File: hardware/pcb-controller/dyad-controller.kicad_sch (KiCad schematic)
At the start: 36 parts, among them J1 USB_C_Receptacle_USB2.0, J2 SWD, J3 Conn_01x11, J4 Conn_01x11, J5 Conn_01x11, SW1 SW_Push, U1 W25Q128JVS, U2 USBLC6-2SC6, U3 RP2040, U4 XC6206PxxxMR-Regulator_Linear, Y1 12MHz

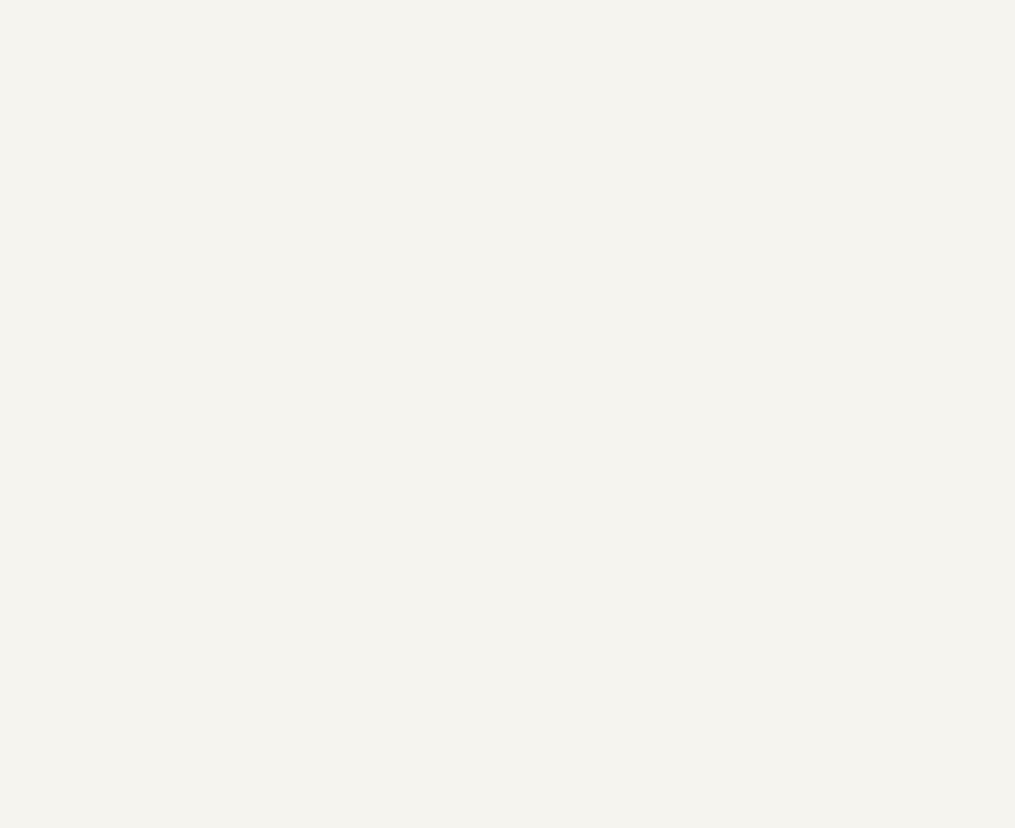
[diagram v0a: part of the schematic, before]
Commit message: Add both main FFC connectors to the controller schematic
J6 (left half) and J7 (right half), Connector_Generic:Conn_01x20 against the
C19273932 footprint, all 40 pins wired. The `dyad` library is registered in
the controller's fp-lib-table with the same relative URI the mains use.

Both carry the same net-to-pad assignment, derived pad by pad as
`pad m = main pin (21 - m)` rather than transcribed:

  1=HAND(GPIO12)  2=+3V3  3-10=COL7..COL0(GPIO26..19)
  11-15=ROW0..ROW4(GPIO14..18)  16,18=GND  17=LEDIN(GPIO13)  19,20=+5V

The 5 V pins land on **+5V, not VBUS**. VBUS -> F1 -> +5V, so +5V is the
fused rail, and §3 already notes the fuse is deliberately in the LED path --
which is the whole reason it needs upsizing if RGB is populated. Taking the
FFC's 5 V from VBUS would have put the LED current outside the fuse and
quietly defeated that. Verified by reading the net back: +5V now contains
F1 pin 2, the LDO input, the ESD part, the PWR_FLAG and both connectors.

The sheet moved A4 -> A3. Placed content already ran to x=282.6 on a 297 mm
frame, and two 20-pin connectors need 48 mm of pin span each, with the knob
FFC and second USB-C still to come.

This also corrects the pad table added in 4bcd259, which was garbled: it
repeated COL0-6 in both halves and omitted ROW3, ROW4, both GNDs, LEDIN and
both VCCs. It carried a "not verified" warning, which is the only reason it
did not reach copper. The corrected table gives the controller's own net
name per pad and carries a count check.

Numbers: ERC is byte-identical to baseline -- 192 violations, 0 errors, and
not one mentions J6 or J7. 40 pins added with no new findings. 0 shorts, 0
orphans. The 4 symbol overlaps are pre-existing in the vendored reference
design and involve none of the new parts.

Still open, deliberately: whether one or both connectors are populated per
board, and whether the dev-board headers J3/J4/J5 survive -- three 1x11
through-hole headers are hard to fit on a 50 x 35 board that also needs two
FFCs an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
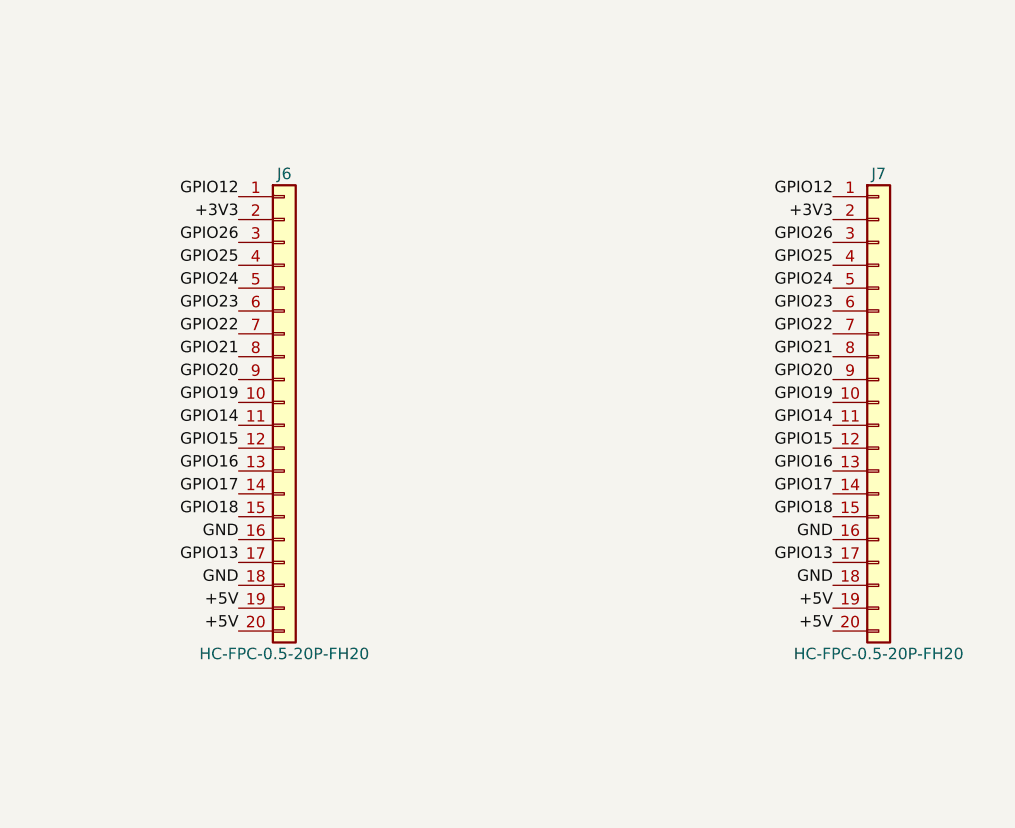
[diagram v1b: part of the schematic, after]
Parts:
- added J6, J7: HC-FPC-0.5-20P-FH20, dyad:FPC-SMD_20P-P0.50_HC-FPC-0.5-20P-FH20, symbol Connector_Generic:Conn_01x20
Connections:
- net +3V3: now also J6.2 (Pin_2), J7.2 (Pin_2)
- net +5V: now also J6.19 (Pin_19), J6.20 (Pin_20), J7.19 (Pin_19), J7.20 (Pin_20)
- net GND: now also J6.16 (Pin_16), J6.18 (Pin_18), J7.16 (Pin_16), J7.18 (Pin_18)
- net GPIO12: now also J6.1 (Pin_1), J7.1 (Pin_1)
- net GPIO13: now also J6.17 (Pin_17), J7.17 (Pin_17)
- net GPIO14: now also J6.11 (Pin_11), J7.11 (Pin_11)
- net GPIO15: now also J6.12 (Pin_12), J7.12 (Pin_12)
- net GPIO16: now also J6.13 (Pin_13), J7.13 (Pin_13)
- net GPIO17: now also J6.14 (Pin_14), J7.14 (Pin_14)
- net GPIO18: now also J6.15 (Pin_15), J7.15 (Pin_15)
- net GPIO19: now also J6.10 (Pin_10), J7.10 (Pin_10)
- net GPIO20: now also J6.9 (Pin_9), J7.9 (Pin_9)
- net GPIO21: now also J6.8 (Pin_8), J7.8 (Pin_8)
- net GPIO22: now also J6.7 (Pin_7), J7.7 (Pin_7)
- net GPIO23: now also J6.6 (Pin_6), J7.6 (Pin_6)
- net GPIO24: now also J6.5 (Pin_5), J7.5 (Pin_5)
- net GPIO25: now also J6.4 (Pin_4), J7.4 (Pin_4)
- net GPIO26: now also J6.3 (Pin_3), J7.3 (Pin_3)

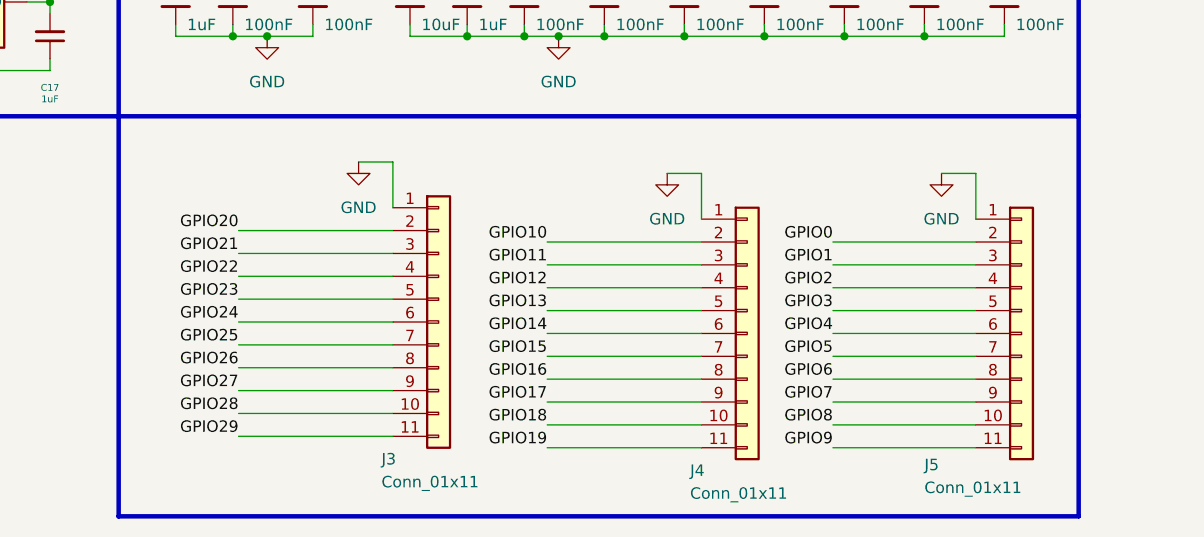
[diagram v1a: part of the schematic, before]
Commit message: Delete the reference design's J3/J4/J5 breakout headers
Three 1x11 through-hole pin sockets inherited from the RP2040 dev board.
They are a Pico-style GPIO breakout; this board reaches the halves over FFC
instead, and three headers is ~84 mm of edge on a 50 x 35 board that must
also carry two FFCs and two USB-C. CONTROLLER.md §4 already listed the
deletion as unconditional change 4 and §5 as schematic step 1.

Checked before deleting: all three carried only GND and GPIO nets -- no
power rails, pull-ups or straps -- so nothing unique was lost.

Removed with them, after tracing each: 33 wire stubs, 30 now-floating GPIO
labels, and 3 GND power symbols (#PWR028/29/30) that fed nothing else. The
GPIO nets keep their names because each had a second label at the RP2040
pin. Orphan check is back to 0.

**This leaves 15 ERC errors, deliberately, and they are the map of what is
still missing.** Each header was the second connection on its GPIO net, so
15 nets now reach only the MCU pin: pin_not_driven and isolated_pin_label on
GPIO0-11 and GPIO27-29. GPIO0-10 clear with the knob FFC, GPIO11 with the
second USB-C, and GPIO27-29 are the three genuine spares that want
no-connect flags once confirmed final.

Nothing else regressed, and two counts improved because the headers took
their own off-grid pins with them: endpoint_off_grid 136 -> 94,
lib_symbol_mismatch 52 -> 49. Symbols 73 -> 67. J1 (USB-C), J2 (SWD) and the
new J6/J7 are untouched; J2 stays because SWD is worth keeping for bring-up.

Co-Authored-By: Claude Opus 5 <noreply@anthropic.com>
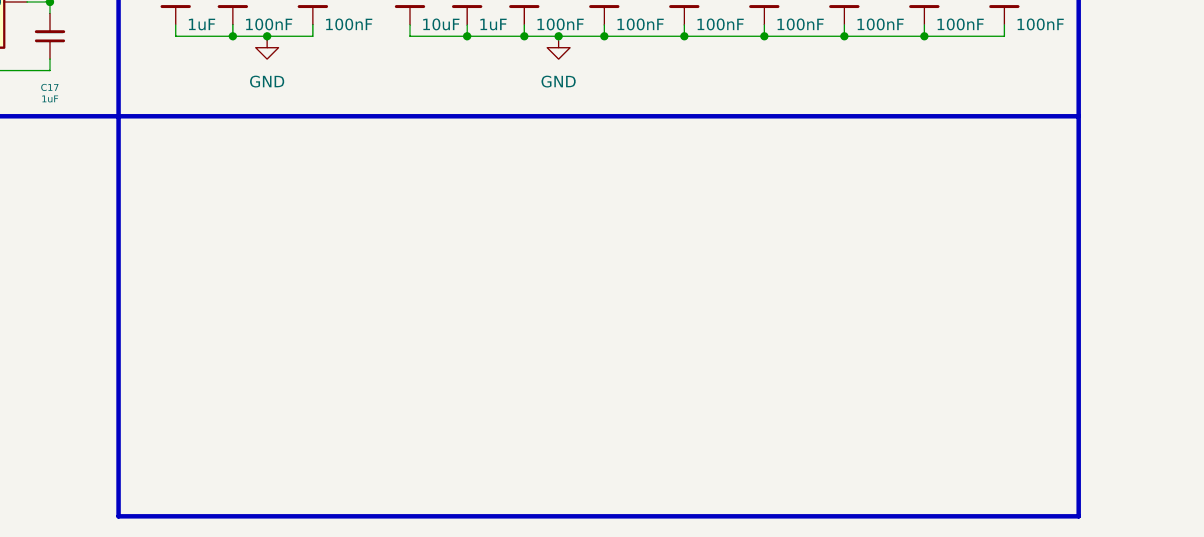
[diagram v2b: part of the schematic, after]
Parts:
- removed J3, J4, J5: Conn_01x11, Connector_PinSocket_2.54mm:PinSocket_1x11_P2.54mm_Vertical, symbol Connector_Generic:Conn_01x11

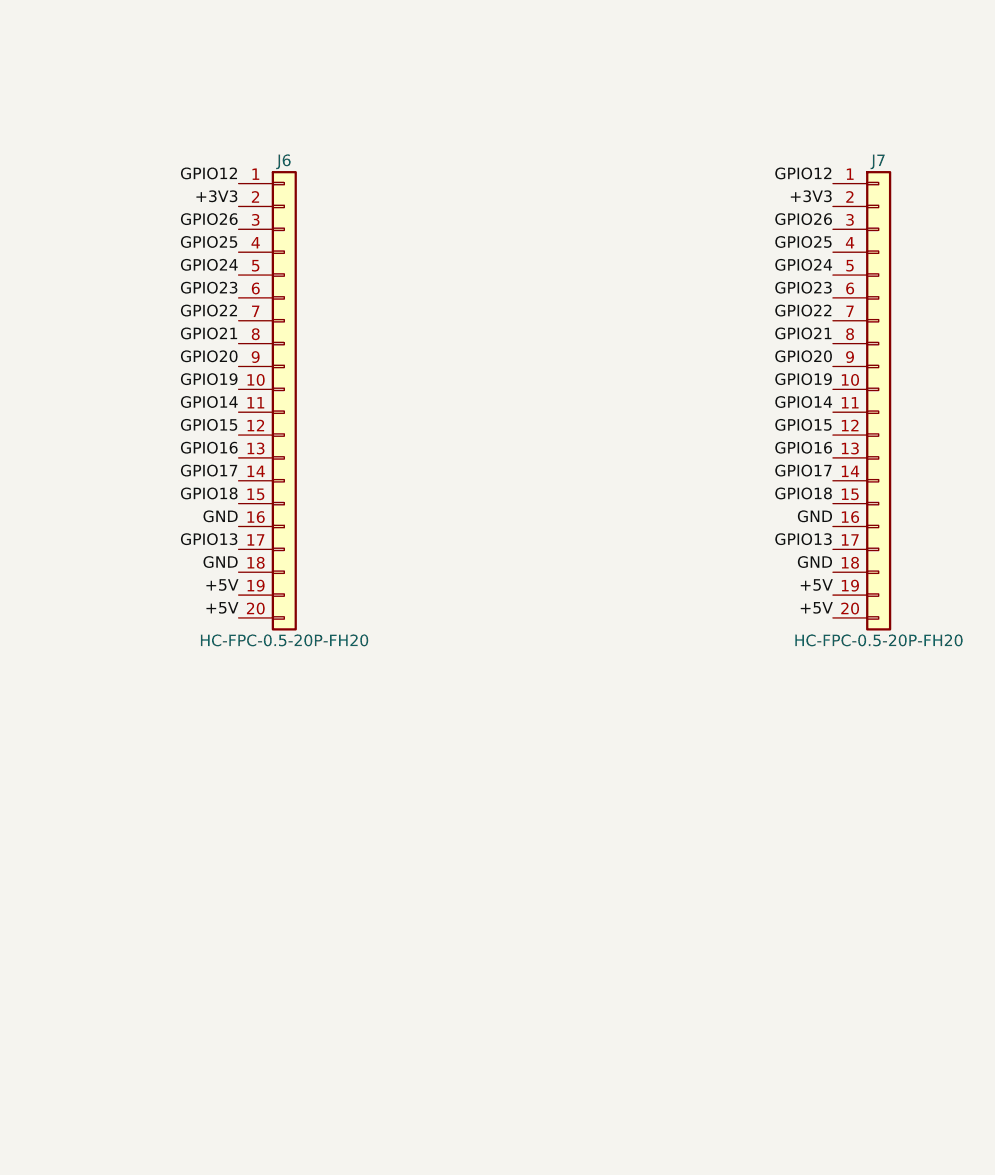
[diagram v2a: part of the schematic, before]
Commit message: Add the knob FFC to the controller schematic
J8, Connector_Generic:Conn_01x14 against a newly pulled C19273929
footprint, all 14 pins wired per CONTROLLER.md §2:

  1=+3V3  2,14=GND  3=SCK(GPIO2)  4=MOSI(GPIO3)  5=D0(GPIO0)  6=D1(GPIO1)
  7=CS(GPIO4)  8=DC(GPIO5)  9=RST(GPIO6)  10=BL(GPIO7)  11=DR(GPIO8)
  12=ENC_A(GPIO9)  13=ENC_B(GPIO10)

**This clears 11 of the 15 ERC errors that deleting J3/J4/J5 exposed.**
Errors 15 -> 4. The remaining four are exactly the ones predicted when the
headers went: GPIO11, which clears with the second USB-C, and GPIO27-29,
the three genuine spares that want no-connect flags once confirmed final.
Nothing else moved -- endpoint_off_grid 94, lib_symbol_mismatch 49, the
same 4 symbol overlaps inherited from the vendored design, 0 shorts, 0
orphans.

The §2 knob table is now explicitly labelled as the CONTROLLER's numbering.
It had the same ambiguity that made the main-FFC table dangerous: a bare
"#" column in the controller's own document. The knob module does not exist
yet, so it will be designed to match -- its pads are the reverse,
`knob pad m = controller pin (15 - m)`, same relation and same reason as
the main link.

Footprint pulled and corrected the same way as the 20-pin: format upgraded
from legacy, .step deleted, model path made relative, hold-down tabs
renamed MP (numbered 15/16 here rather than 21/22 -- the numbers follow the
position count). Geometry verified against the source package data: 14 pads
0.300 x 1.500 at 0.5 mm pitch, 6.500 span, pin 1 left, MP pads 2.000 x
1.700 at x=+-4.950 and dy +2.600, all SMD, courtyard present -- consistent
with the 20-pin sibling throughout.

One defect did NOT recur: this pull emitted `(attr smd)` already. Recorded
in MANUAL_TASKS.md so the checklist says verify rather than assume.

Co-Authored-By: Claude Opus 5 <noreply@anthropic.com>
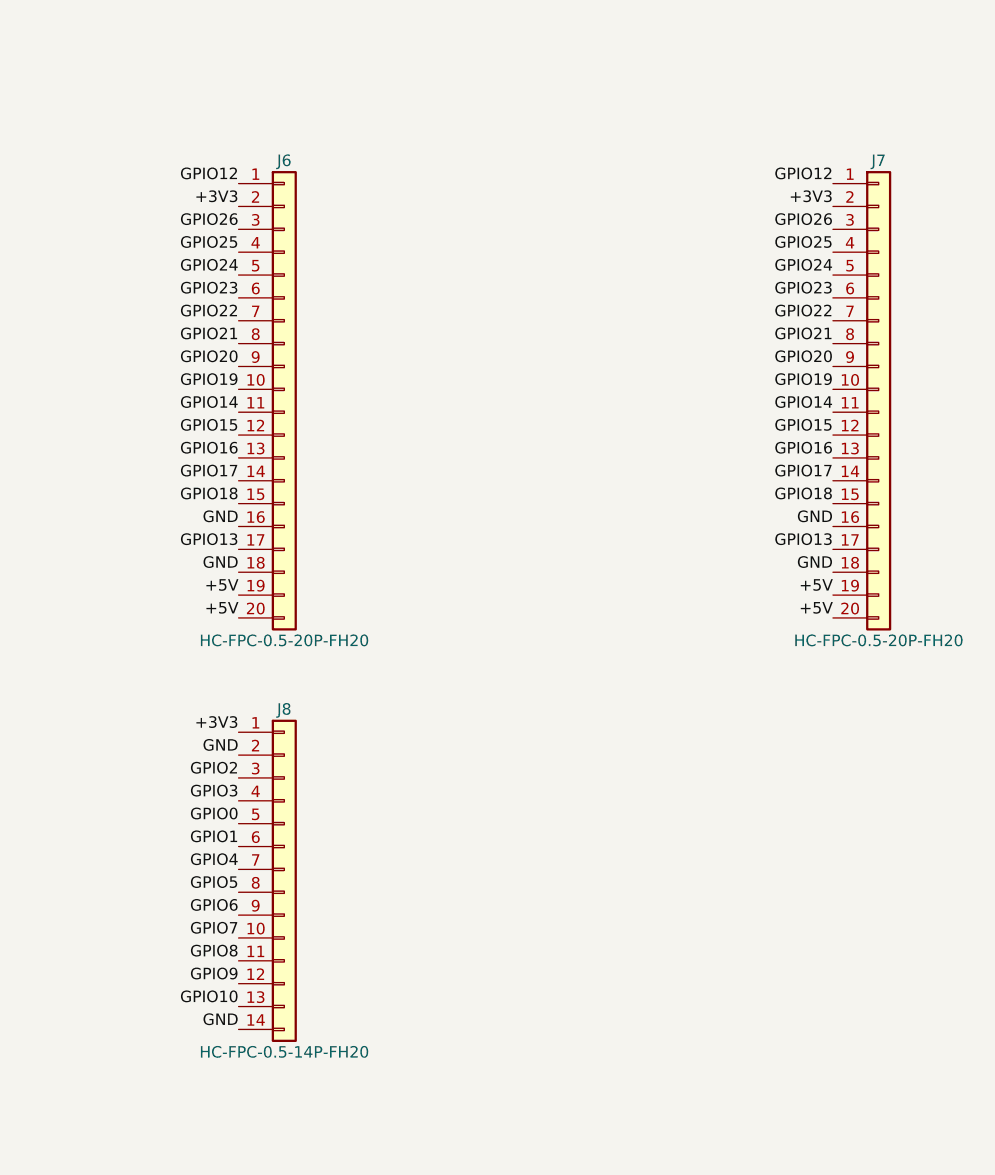
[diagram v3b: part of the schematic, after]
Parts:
- added J8: HC-FPC-0.5-14P-FH20, dyad:FPC-SMD_14P-P0.50_HC-FPC-0.5-14P-FH20, symbol Connector_Generic:Conn_01x14
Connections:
- net +3V3: now also J8.1 (Pin_1)
- net GND: now also J8.14 (Pin_14), J8.2 (Pin_2)
- net GPIO0: now also J8.5 (Pin_5)
- net GPIO1: now also J8.6 (Pin_6)
- net GPIO10: now also J8.13 (Pin_13)
- net GPIO2: now also J8.3 (Pin_3)
- net GPIO3: now also J8.4 (Pin_4)
- net GPIO4: now also J8.7 (Pin_7)
- net GPIO5: now also J8.8 (Pin_8)
- net GPIO6: now also J8.9 (Pin_9)
- net GPIO7: now also J8.10 (Pin_10)
- net GPIO8: now also J8.11 (Pin_11)
- net GPIO9: now also J8.12 (Pin_12)
